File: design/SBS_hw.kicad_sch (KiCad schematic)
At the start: 18 parts

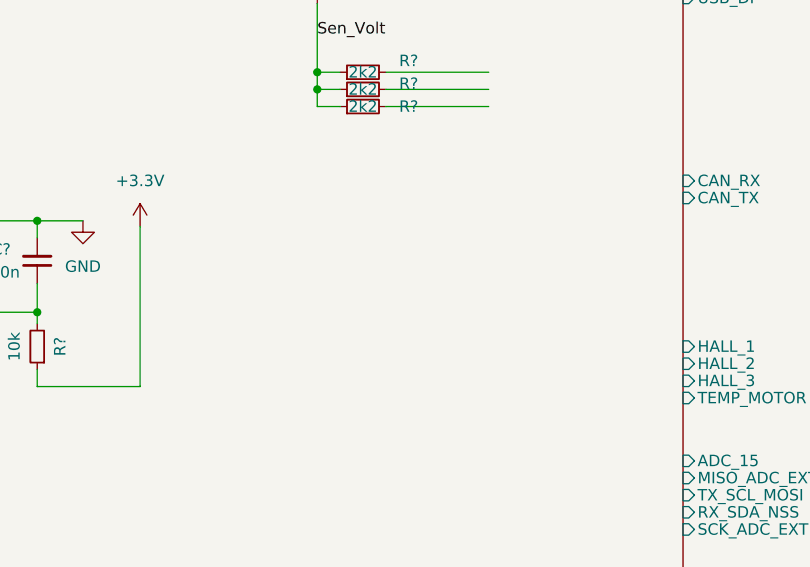
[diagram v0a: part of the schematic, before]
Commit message: reverted back to an older version (more stable) of kicad, so needed to start from an old copy
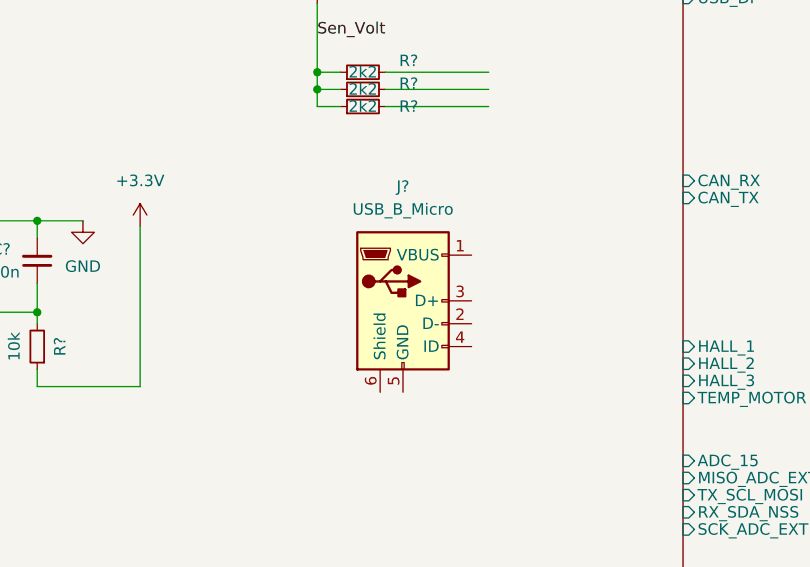
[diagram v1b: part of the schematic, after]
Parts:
- added J?: USB_B_Micro, symbol Connector:USB_B_Micro
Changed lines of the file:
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@@
     (pin "1")
+  )
+  (symbol (lib_id "Connector:USB_B_Micro") (at 97.79 67.31 0) (unit 1)
+    (in_bom yes) (on_board yes) (fields_autoplaced)
+    (property "Reference" "J?" (id 0) (at 97.79 54.61 0))
+    (property "Value" "USB_B_Micro" (id 1) (at 97.79 57.15 0))
+    (property "Footprint" "" (id 2) (at 101.6 68.58 0)
+      (effects (font (size 1.27 1.27)) hide)
+    )
+    (property "Datasheet" "~" (id 3) (at 101.6 68.58 0)
+      (effects (font (size 1.27 1.27)) hide)
+    )
+    (pin "1")
+    (pin "2")
+    (pin "3")
+    (pin "4")
+    (pin "5")
+    (pin "6")
   )
   (symbol (lib_id "power:GND") (at 67.31 154.94 0) (unit 1)
@@
       (reference "FB?") (unit 1) (value "FCM1608KF-601T05") (footprint "Inductor_SMD:L_0603_1608Metric_Pad1.05x0.95mm_HandSolder")
     )
+    (path "/046359fa-3971-4114-9fb9-e8d438d0e47e"
+      (reference "J?") (unit 1) (value "USB_B_Micro") (footprint "")
+    )
     (path "/1f25b647-d4a6-4edc-b12f-b20d6ceaa2d7"

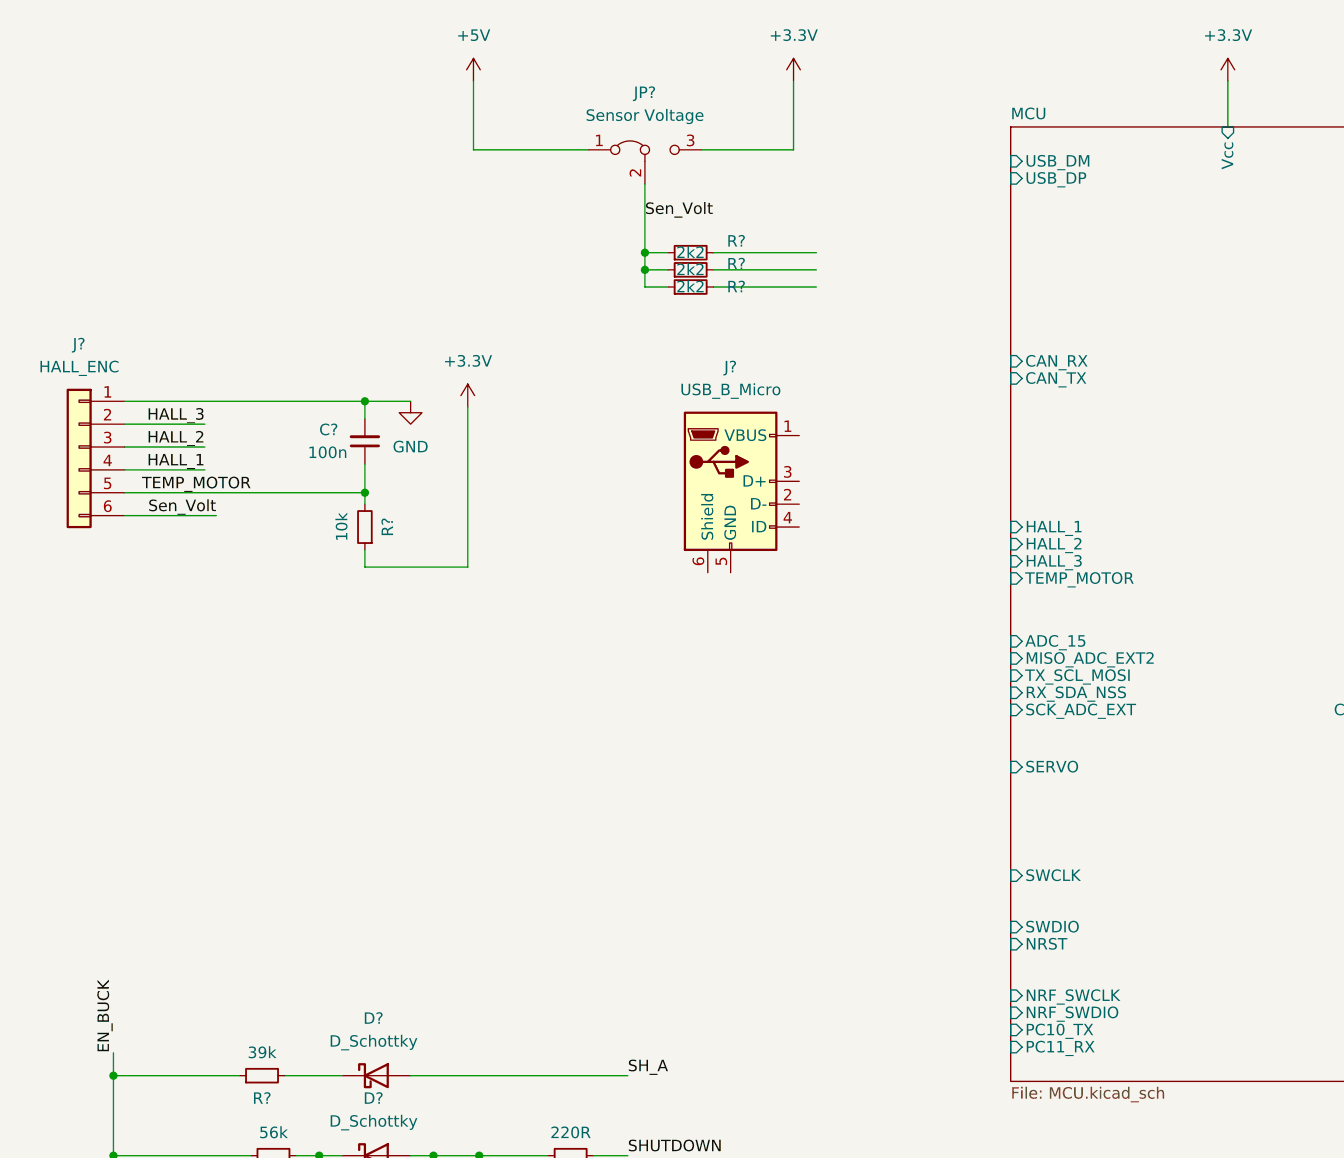
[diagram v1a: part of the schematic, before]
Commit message: added some connectors:
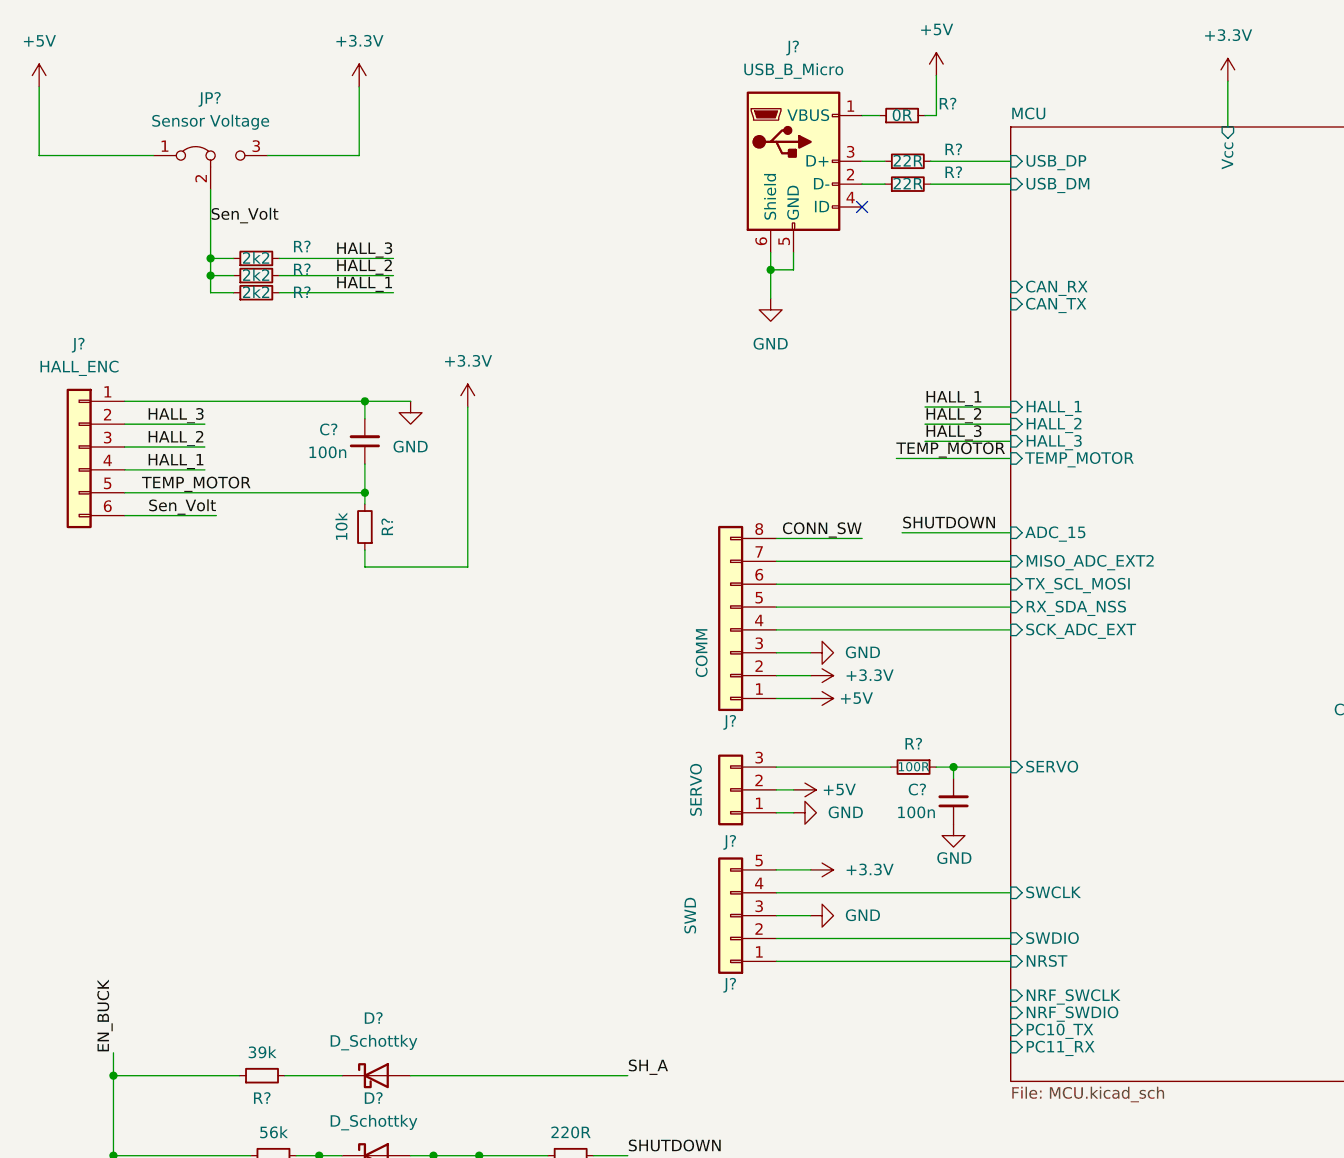
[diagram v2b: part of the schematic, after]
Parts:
- added C?: 100n, Capacitor_SMD:C_0603_1608Metric_Pad1.08x0.95mm_HandSolder, symbol Device:C_Small
- added J?: SERVO, symbol Connector_Generic:Conn_01x03
- added J?: COMM, symbol Connector_Generic:Conn_01x08
- added J?: SWD, symbol Connector_Generic:Conn_01x05
- added R? (x2): 22R, Resistor_SMD:R_0603_1608Metric_Pad0.98x0.95mm_HandSolder, symbol Device:R_Small
- added R?: 0R, Resistor_SMD:R_0603_1608Metric_Pad0.98x0.95mm_HandSolder, symbol Device:R_Small
- added R?: 100R, Resistor_SMD:R_0603_1608Metric_Pad0.98x0.95mm_HandSolder, symbol Device:R_Small
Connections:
- net +3.3V: now also J?.2 (Pin_2), J?.5 (Pin_5)
- net +5V: now also J?.1 (Pin_1), J?.2 (Pin_2), R?.2
- net CONN_SW: now also J?.8 (Pin_8)
- net GND: now also J?.5 (GND), J?.6 (Shield), C?.1, J?.1 (Pin_1), J?.3 (Pin_3), J?.3 (Pin_3)
- net HALL_1: now also R?.2
- net HALL_2: now also R?.2
- net HALL_3: now also R?.2
- net MCU/MISO_ADC_EXT2: now also J?.7 (Pin_7)
- net MCU/NRST: now also J?.1 (Pin_1)
- net MCU/RX_SDA_NSS: now also J?.5 (Pin_5)
- net MCU/SCK_ADC_EXT: now also J?.4 (Pin_4)
- net MCU/SERVO: now also C?.2, R?.1
- net MCU/SWCLK: now also J?.4 (Pin_4)
- net MCU/SWDIO: now also J?.2 (Pin_2)
- net MCU/TX_SCL_MOSI: now also J?.6 (Pin_6)
- net MCU/USB_DM: now also R?.2
- net MCU/USB_DP: now also R?.2
- net at J?.1 (VBUS): now also R?.1
- net at J?.2 (D-): now also R?.1
- net at J?.3 (D+): now also R?.1
- new net: J?.3 (Pin_3), R?.2
- no-connect marks 0 -> 1
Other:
- moved on the sheet: J?, JP?, R?

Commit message: updates to BLDC
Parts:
- added C?: 2u2, Capacitor_SMD:C_0603_1608Metric_Pad1.08x0.95mm_HandSolder, symbol Device:C_Small
- added D?: RED, symbol Device:LED
- added J?: CAN, symbol Connector_Generic:Conn_01x04
- added R?: 1k, Resistor_SMD:R_0603_1608Metric_Pad0.98x0.95mm_HandSolder, symbol Device:R_Small
- added U?: EYSGJNZWY, BLE_EYSGJNZWY, symbol EYSGJNZWY:EYSGJNZWY
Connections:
- net +3.3V: now also C?.2, U?.5 (VCC_NRF), U?.6 (AVDD)
- net +5V: now also J?.4 (Pin_4)
- net GND: now also C?.1, D?.1 (K), J?.1 (Pin_1), U?.1 (GND), U?.12 (GND), U?.15 (GND), U?.20 (GND), U?.28 (GND), U?.9 (GND)
- net MCU/NRF_SWCLK: now also U?.17 (SWDCLK)
- net MCU/NRF_SWDIO: now also U?.16 (SWDIO)
- net MCU/PC10_TX: now also U?.21 (P0.01_AIN2)
- net MCU/PC11_RX: now also U?.22 (P0.02_AIN3)
- new net: D?.2 (A), R?.1
- new net: R?.2, U?.19 (P0.03_AIN4)
- new net: U?.13 (OUT_ANT), U?.14 (OUT_MOD)
- new net CAN/CANH: J?.3 (Pin_3)
- new net CAN/CANL: J?.2 (Pin_2)
- no-connect marks 1 -> 14
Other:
- added sheet CAN (CAN.kicad_sch)
- sheet DRV8301 ports: added CS, EN_BUCK, EN_GATE, FAULT, GH_A, GH_B, GH_C, GL_A, GL_B, GL_C, INH_A, INH_B, INH_C, INL_A, INL_B, INL_C, SCLK, SDI, SDO, SH_A, SH_B, SH_C, SL_A, SL_B, SL_C, SUPPLY; removed none
- moved on the sheet: C?, D?, J?, R?
